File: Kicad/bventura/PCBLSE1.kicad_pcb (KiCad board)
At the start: 4 copper layers, 70 x 90 mm, 83 parts, among them IC1 LM339D, IC2 IR2301SPBF, IC3 IR2301SPBF, IC4 IR2301SPBF, IC5 LMS8117AMP-3.3_NOPB, J1 Conn_02x10_Counter_Clockwise, J10 Conn_01x04, J11 Conn_01x04, J12 Conn_01x04, J13 Conn_01x05, J14 Conn_01x02, J15 Conn_01x02_Pin, J16 Conn_01x04, J17 Conn_01x02, J18 Conn_01x04, J2 Conn_02x10_Counter_Clockwise, J3 Conn_01x02, J4 Conn_01x02, J5 Conn_01x02, J6 Conn_01x02, J7 Conn_01x03, J8 Conn_01x03, J9 Conn_01x05, Q1 Q_NMOS_GDS, Q2 Q_NMOS_GDS, Q3 Q_NMOS_GDS, Q4 Q_NMOS_GDS, Q5 Q_NMOS_GDS, Q7 Q_NMOS_GDS, U1 L7805

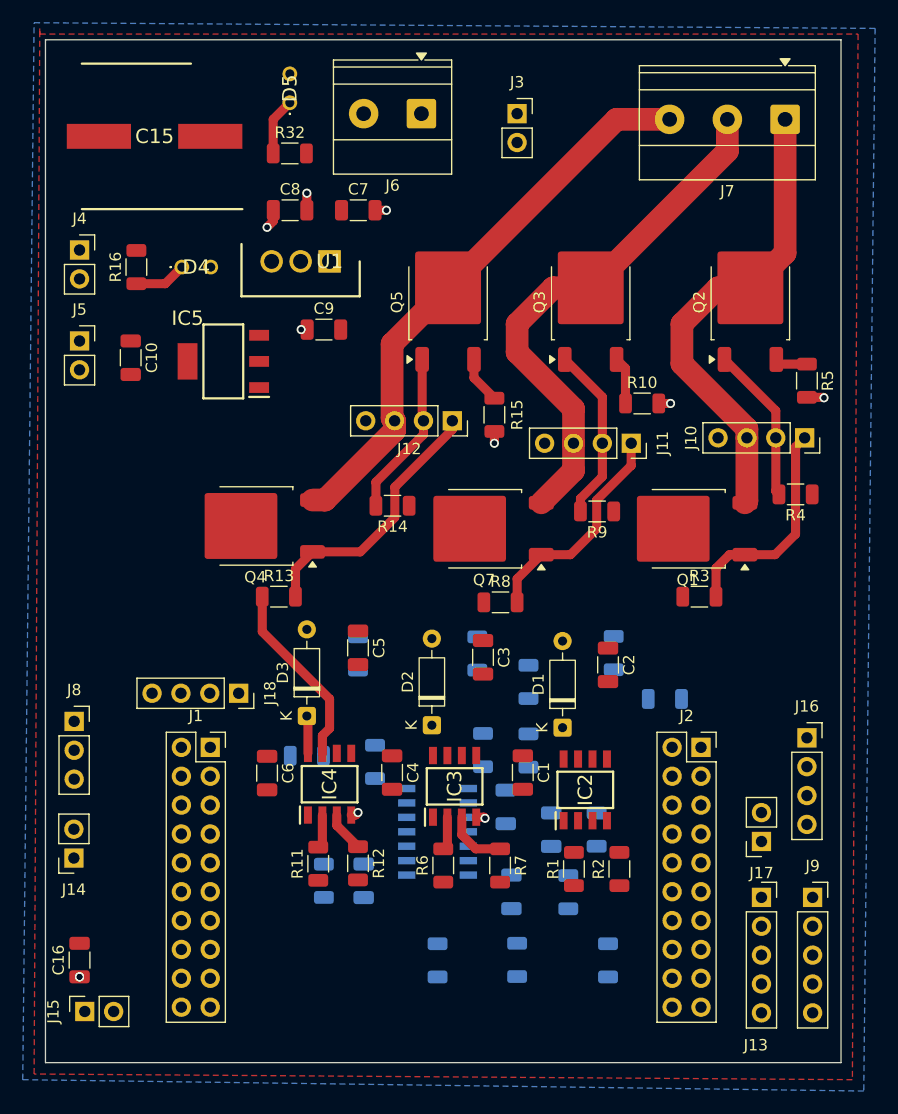
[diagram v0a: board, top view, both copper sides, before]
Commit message: Errors corregits
Errors corregits de l'esquema i nou placement dels drivers de potència. DRC esquema 3 errors, relacionats amb el power flag.
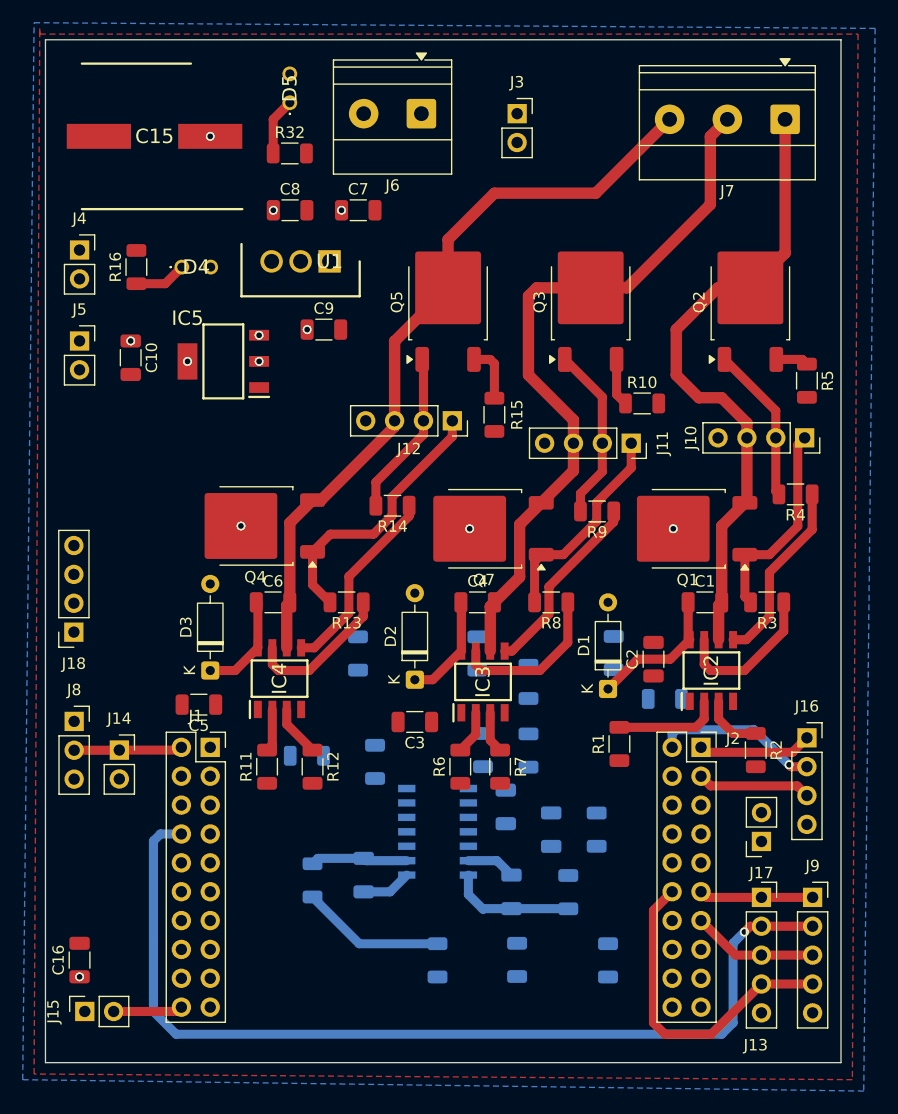
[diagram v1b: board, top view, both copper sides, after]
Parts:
- moved C1 21.9 mm to (99.5, 69.0), turned to 0 degrees
- moved C4 16.8 mm to (79.5, 69.0), turned to 0 degrees
- moved R2 15.9 mm to (104.0, 82.0), turned to -90 degrees
- moved J18 15.5 mm to (44.0, 71.6), turned to 180 degrees
- moved IC2 15.3 mm to (100.1, 75.0)
- moved C6 15.0 mm to (61.5, 69.0), turned to 0 degrees
- moved C5 14.9 mm to (55.0, 78.0), turned to 180 degrees
- moved R1 11.7 mm to (92.0, 81.5)
- moved J14 10.3 mm to (48.0, 82.0), turned to 0 degrees
- moved IC4 10.3 mm to (62.1, 75.7)
- moved R11 9.65 mm to (61.0, 83.5)
- moved IC3 9.52 mm to (80.0, 76.0)
- moved D3 9.39 mm to (56.0, 75.0)
- moved R12 9.39 mm to (65.0, 83.5)
- moved R6 8.82 mm to (78.0, 83.5)
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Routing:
- net MOSI: track 0.00 -> 84.6 mm, vias 0 -> 1
- net /SS: track 0.00 -> 28.5 mm
- net /LOC: track 0.00 -> 17.1 mm
- net FASE_B: track 46.6 -> 63.4 mm
- net /LOB: track 0.00 -> 16.6 mm
- net /LOA: track 0.00 -> 16.3 mm
- net FASE_C: track 50.1 -> 66.1 mm
- net FASE_A: track 41.6 -> 56.2 mm
- net BMEFB_ZERO: track 0.00 -> 14.6 mm, vias 0 -> 1
- net /HOB: track 0.00 -> 14.1 mm
- net /HOA: track 0.00 -> 13.4 mm
- net FASE_C_RED: track 0.00 -> 12.7 mm
- net /VBA: track 0.00 -> 12.3 mm
- net MISO: track 0.00 -> 11.1 mm
- net /NON_INVA: track 0.00 -> 11.1 mm
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
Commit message: Add files via upload
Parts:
- removed J18: Conn_01x04, Connector_PinSocket_2.54mm:PinSocket_1x04_P2.54mm_Vertical
- moved R18 7.91 mm to (75.0, 80.0)
- moved R20 7.63 mm to (92.0, 84.0), turned to 90 degrees
- moved R17 7.42 mm to (88.0, 80.0)
- moved R19 4.44 mm to (67.0, 77.5)
- moved R25 3.57 mm to (74.0, 103.5)
- moved C11 2.81 mm to (82.5, 97.3)
- moved C12 2.81 mm to (86.0, 91.8)
- moved C13 2.81 mm to (69.5, 95.8)
- moved IC1 2.81 mm to (76.0, 92.0)
- moved R26 2.81 mm to (87.5, 97.3)
- moved R27 2.81 mm to (90.0, 91.8)
- moved R23 2.81 mm to (83.0, 103.3)
- moved R28 2.81 mm to (65.0, 96.3)
- moved C14 2.00 mm to (82.0, 89.0)
- moved C16 1.50 mm to (46.0, 100.5)
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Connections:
- C15 pad 1: +5V -> VCC
- D5 pad 2: +5V -> VCC
- J1 pad 1: unconnected-(J1-Pin_1-Pad1) -> /JPP_V
- J1 pad 10: HAI -> unconnected-(J1-Pin_10-Pad10)
- J1 pad 11: LAI -> BMEFC_ZERO
- J1 pad 16: unconnected-(J1-Pin_16-Pad16) -> MOSI
- J1 pad 17: HBI -> unconnected-(J1-Pin_17-Pad17)
- J1 pad 18: LBI -> unconnected-(J1-Pin_18-Pad18)
- J1 pad 19: GND -> unconnected-(J1-Pin_19-Pad19)
- J1 pad 2: DUTY -> unconnected-(J1-Pin_2-Pad2)
- J1 pad 20: /JPP_V -> unconnected-(J1-Pin_20-Pad20)
- J1 pad 3: unconnected-(J1-Pin_3-Pad3) -> GND
- J1 pad 4: unconnected-(J1-Pin_4-Pad4) -> DUTY
- J1 pad 5: unconnected-(J1-Pin_5-Pad5) -> LCI
- J1 pad 7: unconnected-(J1-Pin_7-Pad7) -> HBI
- J1 pad 8: MOSI -> unconnected-(J1-Pin_8-Pad8)
- J2 pad 1: BMEFA_ZERO -> unconnected-(J2-Pin_1-Pad1)
- J2 pad 10: unconnected-(J2-Pin_10-Pad10) -> LAI
- J2 pad 11: SCLK -> unconnected-(J2-Pin_11-Pad11)
- J2 pad 12: /SS -> BMEFB_ZERO
- J2 pad 13: MISO -> unconnected-(J2-Pin_13-Pad13)
- J2 pad 15: unconnected-(J2-Pin_15-Pad15) -> MISO
- J2 pad 17: unconnected-(J2-Pin_17-Pad17) -> /SS
- J2 pad 19: unconnected-(J2-Pin_19-Pad19) -> SCLK
- J2 pad 2: BMEFB_ZERO -> HCI
- J2 pad 3: BMEFC_ZERO -> unconnected-(J2-Pin_3-Pad3)
- J2 pad 4: LCI -> LBI
- J2 pad 5: HCI -> unconnected-(J2-Pin_5-Pad5)
- J2 pad 6: unconnected-(J2-Pin_6-Pad6) -> BMEFA_ZERO
- J2 pad 8: unconnected-(J2-Pin_8-Pad8) -> HAI
- J6 pad 2: +5V -> GND
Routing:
- net MOSI: track 84.6 -> 0.00 mm, vias 1 -> 0
- net /SS: track 28.5 -> 0.00 mm
- net FASE_B: track 63.4 -> 37.0 mm
- net FASE_C: track 66.1 -> 41.2 mm
- net GHC: track 23.9 -> 0.00 mm
- net GHB: track 18.7 -> 0.00 mm
- net GHA: track 18.1 -> 0.00 mm
- net /LOC: track 17.1 -> 0.00 mm
- net FASE_A: track 56.2 -> 39.3 mm
- net /LOB: track 16.6 -> 0.00 mm
- net /LOA: track 16.3 -> 0.00 mm
- net GLB: track 15.5 -> 0.00 mm
- net BMEFB_ZERO: track 14.6 -> 0.00 mm, vias 1 -> 0
- net /HOB: track 14.1 -> 0.00 mm
- net GLA: track 13.9 -> 0.00 mm
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
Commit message: Add files via upload
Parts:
- moved J16 64.1 mm to (45.5, 69.2)
- moved J17 61.2 mm to (45.0, 104.2)
- moved C16 19.0 mm to (61.5, 89.5)
- moved J15 11.5 mm to (45.5, 93.5)
- moved J13 10.1 mm to (104.0, 105.0), turned to 180 degrees
- moved J9 10.1 mm to (108.5, 105.0), turned to 180 degrees
- moved R30 6.02 mm to (84.0, 86.5), turned to 0 degrees
- moved J14 4.27 mm to (49.5, 86.0)
- moved J8 4.14 mm to (45.0, 83.5)
- moved R26 3.72 mm to (87.0, 101.0), turned to 90 degrees
- moved R28 3.46 mm to (66.0, 93.0), turned to 90 degrees
- moved R23 3.01 mm to (80.0, 103.5)
- moved C12 2.71 mm to (85.5, 94.5), turned to 90 degrees
- moved R11 2.50 mm to (63.5, 83.5)
- moved C14 2.12 mm to (83.5, 90.5), turned to 0 degrees
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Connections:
- J1 pad 13: unconnected-(J1-Pin_13-Pad13) -> BMEFB_ZERO
- J1 pad 5: LCI -> HCI
- J1 pad 7: HBI -> LCI
- J2 pad 10: LAI -> HBI
- J2 pad 12: BMEFB_ZERO -> unconnected-(J2-Pin_12-Pad12)
- J2 pad 2: HCI -> LAI
- J2 pad 4: LBI -> HAI
- J2 pad 8: HAI -> LBI
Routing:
- net VN_RED: track 0.00 -> 81.9 mm, vias 0 -> 2
- net BMEFA_ZERO: track 0.00 -> 78.2 mm, vias 0 -> 3
- net BMEFB_ZERO: track 0.00 -> 74.3 mm, vias 0 -> 2
- net MOSI: track 0.00 -> 70.3 mm, vias 0 -> 2
- net BMEFC_ZERO: track 0.00 -> 55.6 mm, vias 0 -> 4
- net FASE_A_RED: track 0.00 -> 39.1 mm, vias 0 -> 4
- net FASE_B_RED: track 0.00 -> 38.2 mm, vias 0 -> 2
- net FASE_A: track 39.3 -> 74.2 mm, vias 0 -> 1
- net FASE_C_RED: track 0.00 -> 34.4 mm
- net VCC: track 5.54 -> 35.3 mm, vias 4 -> 19
- net FASE_B: track 37.0 -> 66.6 mm, vias 0 -> 1
- net FASE_C: track 41.2 -> 70.8 mm, vias 0 -> 1
- net GHC: track 0.00 -> 24.6 mm
- net /JPP_V: track 0.00 -> 21.9 mm, vias 0 -> 2
- net HBI: track 0.00 -> 21.5 mm
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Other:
- board text added: "${REFERENCE}"

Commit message: Add files via upload
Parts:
- moved R2 1.50 mm to (105.5, 82.0)
- moved IC2 0.50 mm to (100.1, 74.5)
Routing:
- net VCC: track 35.3 -> 40.0 mm
- net FASE_A: track 74.2 -> 71.8 mm
- net /LINA: track 8.66 -> 6.88 mm
- net /HOA: track 13.0 -> 11.9 mm
- net LAI: track 10.2 -> 11.1 mm
- net FASE_C_RED: track 34.4 -> 35.3 mm, vias 0 -> 2
- net /HINA: track 10.2 -> 9.34 mm
- net /VBA: track 12.3 -> 12.9 mm
- net FASE_B: track 66.6 -> 66.1 mm

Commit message: versió final kicad
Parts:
- added G***: LOGO, logos:logo_UB, F.Cu at (83.0, 104.5)
- added G***: LOGO, logos:rammstein, B.Cu at (102.5, 72.0)
- added G***: LOGO, logos:logo_akatsuki, B.Cu at (54.0, 34.0)
- J1, J2: footprint Connector_PinSocket_2.54mm:PinSocket_2x10_P2.54mm_Vertical -> Connector_PinHeader_2.54mm:PinHeader_2x10_P2.54mm_Vertical
- moved J5 10.2 mm to (46.5, 56.0), turned to 180 degrees
- moved J8 4.55 mm to (48.0, 86.9)
- moved J7 4.53 mm to (102.1, 27.0)
- moved J14 4.27 mm to (48.0, 82.0), turned to -90 degrees
- moved C7 4.10 mm to (73.0, 35.5)
- moved J15 3.49 mm to (45.8, 97.0)
- moved R32 3.35 mm to (66.0, 31.0)
- moved C8 3.04 mm to (66.0, 35.0)
- moved J6 2.80 mm to (77.0, 27.3)
- moved J2 2.68 mm to (96.5, 81.8)
- moved J1 2.54 mm to (53.5, 81.8)
- moved D5 2.22 mm to (65.0, 24.7)
- moved R5 2.15 mm to (107.0, 51.0), turned to 0 degrees
- moved C15 1.80 mm to (52.6, 29.0)
- moved J10 1.57 mm to (106.8, 55.0)
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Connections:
- J1 pad 1: /JPP_V -> unconnected-(J1-Pin_1-Pad1)
- J1 pad 11: BMEFC_ZERO -> unconnected-(J1-Pin_11-Pad11)
- J1 pad 12: unconnected-(J1-Pin_12-Pad12) -> BMEFC_ZERO
- J1 pad 13: BMEFB_ZERO -> unconnected-(J1-Pin_13-Pad13)
- J1 pad 14: unconnected-(J1-Pin_14-Pad14) -> BMEFB_ZERO
- J1 pad 15: unconnected-(J1-Pin_15-Pad15) -> MOSI
- J1 pad 16: MOSI -> unconnected-(J1-Pin_16-Pad16)
- J1 pad 2: unconnected-(J1-Pin_2-Pad2) -> /JPP_V
- J1 pad 3: GND -> DUTY
- J1 pad 4: DUTY -> GND
- J1 pad 5: HCI -> unconnected-(J1-Pin_5-Pad5)
- J1 pad 6: unconnected-(J1-Pin_6-Pad6) -> HCI
- J1 pad 7: LCI -> unconnected-(J1-Pin_7-Pad7)
- J1 pad 8: unconnected-(J1-Pin_8-Pad8) -> LCI
- J2 pad 1: unconnected-(J2-Pin_1-Pad1) -> LAI
- J2 pad 10: HBI -> unconnected-(J2-Pin_10-Pad10)
- J2 pad 15: MISO -> unconnected-(J2-Pin_15-Pad15)
- J2 pad 16: unconnected-(J2-Pin_16-Pad16) -> MISO
- J2 pad 17: /SS -> unconnected-(J2-Pin_17-Pad17)
- J2 pad 18: unconnected-(J2-Pin_18-Pad18) -> /SS
- J2 pad 19: SCLK -> unconnected-(J2-Pin_19-Pad19)
- J2 pad 2: LAI -> unconnected-(J2-Pin_2-Pad2)
- J2 pad 20: unconnected-(J2-Pin_20-Pad20) -> SCLK
- J2 pad 3: unconnected-(J2-Pin_3-Pad3) -> HAI
- J2 pad 4: HAI -> unconnected-(J2-Pin_4-Pad4)
- J2 pad 5: unconnected-(J2-Pin_5-Pad5) -> BMEFA_ZERO
- J2 pad 6: BMEFA_ZERO -> unconnected-(J2-Pin_6-Pad6)
- J2 pad 7: unconnected-(J2-Pin_7-Pad7) -> LBI
- J2 pad 8: LBI -> unconnected-(J2-Pin_8-Pad8)
- J2 pad 9: unconnected-(J2-Pin_9-Pad9) -> HBI
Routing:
- net VCC: track 40.0 -> 13.4 mm, vias 19 -> 40
- net +3.3V: track 15.9 -> 6.70 mm, vias 9 -> 8
- net BMEFA_ZERO: track 78.2 -> 86.5 mm
- net DUTY: track 9.18 -> 17.3 mm
- net +5V: track 14.3 -> 6.78 mm, vias 9 -> 6
- net FASE_C: track 70.8 -> 64.1 mm
- net FASE_A: track 71.8 -> 67.3 mm
- net /JPP_V: track 21.9 -> 24.9 mm, vias 2 -> 1
- net FASE_B: track 66.1 -> 63.8 mm
- net MOSI: track 70.3 -> 69.1 mm
- net VN_RED: track 81.9 -> 81.0 mm
- net /SLA: track 2.87 -> 3.50 mm
- net /SS: track 13.3 -> 12.8 mm
- net SCLK: track 9.49 -> 8.99 mm
- net MISO: track 9.49 -> 8.99 mm
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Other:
- board text added: "DESIGNED BY Raúl Casado Luque Kevin Brandon Ventura Laura Laboratori de Sistemes Electrònics-1"
- board text added: "Q4"
- board text added: "R6"
- board text removed: "${REFERENCE}"
